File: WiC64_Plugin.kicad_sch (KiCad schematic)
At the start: 59 parts, among them CN1 USERPORT-C64, CN2 OLED0.96, Q1 BSS138, Q10 BSS138, Q11 BSS138, Q2 BSS138, Q3 BSS138, Q4 BSS138, Q5 BSS138, Q6 BSS138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

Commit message: Initial +4 version
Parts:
- removed CN1: USERPORT-C64, WiC64:UPS24CONN, symbol cbm-connectors:USERPORT-C64-CONN
- added CN1: PLUS4_USERPORT, WiC64:UPS24CONN, symbol PLUS4_USERPORT:PLUS4_USERPORT
- SW1: value RESET-C64 -> RESET
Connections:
- net +5V: now also CN1.2 (VCC)
- net FLAG2: now also Q8.3 (D), R16.2, CN1.H (~{DCD}); no longer Q1.3 (D), R2.2
- net GND: now also CN1.1 (GND), CN1.12 (GND), CN1.A (GND), CN1.N (GND)
- net IO14: now also Q4.2 (S), R7.2; no longer Q7.2 (S), R13.2
- net IO16: now also Q1.2 (S), R1.2; no longer Q2.2 (S), R3.2
- net IO17: now also Q11.2 (S), R21.2; no longer Q3.2 (S), R5.2
- net IO18: now also Q2.2 (S), R3.2; no longer Q4.2 (S), R7.2
- net IO21: now also Q7.2 (S), R13.2; no longer Q6.2 (S), R11.2
- net IO22: now also Q9.2 (S), R17.2; no longer Q8.2 (S), R15.2
- net IO23: now also Q10.2 (S), R19.2; no longer Q9.2 (S), R17.2
- net IO25: now also Q6.2 (S), R11.2; no longer Q10.2 (S), R19.2
- net IO26: now also Q8.2 (S), R15.2; no longer Q1.2 (S), R1.2
- net IO27: now also Q3.2 (S), R5.2; no longer Q11.2 (S), R21.2
- net PA2: now also Q3.3 (D), R6.2, CN1.D (~{RTS}); no longer Q11.3 (D), R22.2
- net PB0: now also Q1.3 (D), R2.2, CN1.B (D0); no longer Q2.3 (D), R4.2
- net PB1: now also Q11.3 (D), R22.2, CN1.K (D1); no longer Q3.3 (D), R6.2
- net PB2: now also Q2.3 (D), R4.2, CN1.4 (D2); no longer Q4.3 (D), R8.2
- net PB3: now also CN1.5 (D3)
- net PB4: now also Q7.3 (D), R14.2, CN1.6 (D4); no longer Q6.3 (D), R12.2
- net PB5: now also Q9.3 (D), R18.2, CN1.7 (D5); no longer Q8.3 (D), R16.2
- net PB6: now also Q10.3 (D), R20.2, CN1.J (D6); no longer Q9.3 (D), R18.2
- net PB7: now also Q6.3 (D), R12.2, CN1.F (D7); no longer Q10.3 (D), R20.2
- net PC2: now also Q4.3 (D), R8.2, CN1.E (~{DTR}); no longer Q7.3 (D), R14.2
- net at D4.3: now also CN1.10 (+9VAC)
- net at D4.4: now also CN1.11 (-9VAC)
- net at SW1.1: now also CN1.3 (~{RESET})
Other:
- note added: "+4->ESP"
- note added: "Control Signals Logic: - PC2 : Handshake: C64/+4 => ESP (ack/strobe: byte read from/written to port) (rising edge) - FLAG2: Handshake: ESP => C64/+4 (ack/strobe: byte read from/written to port) (falling edge) - PA2 : Direction: HIGH = C64/+4 => ESP, LOW = ESP => C64/+4 (Controlled by C64/+4)"
- note added: "ESP->+4"
- moved on the sheet: CN2, D3, JP2, SW1

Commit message: Complete changes for +4 version
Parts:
- added L1: FERRITE, WiC64:Ferrite_D6.0mm_L10.00mm_Horizontal, symbol Device:L_Ferrite
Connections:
- net +5V: now also L1.1; no longer CN1.2 (VCC)
- new net: CN1.2 (VCC), L1.2
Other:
- company: (none) -> SukkoPera
- title: WiC64 Plugin -> WiC+4
- moved on the sheet: D3, JP2
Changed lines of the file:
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@@
 	(paper "A4")
 	(title_block
-		(title "WiC64 Plugin")
-		(date "2024-05-26")
-		(rev "0.6-Sukko")
-		(comment 1 "(C) 2021 by GMP")
-		(comment 2 "Modified by SukkoPera 2024")
-		(comment 3 "https://github.com/SukkoPera/WiC64-Plus4")
+		(title "WiC+4")
+		(date "2024-06-02")
+		(rev "1git")
+		(company "SukkoPera")
+		(comment 1 "Based on C64 version by GMP 2021")
+		(comment 2 "https://github.com/SukkoPera/WiC64-Plus4")
 	)
 	(junction
@@
 	)
 	(junction
-		(at 107.95 93.98)
+		(at 101.6 93.98)
 		(diameter 0)
 		(color 0 0 0 0)
@@
 	(wire
 		(pts
-			(xy 96.52 87.63) (xy 96.52 90.17)
+			(xy 92.71 87.63) (xy 92.71 90.17)
 		)
 		(stroke
@@
 	(wire
 		(pts
-			(xy 107.95 93.98) (xy 107.95 88.9)
+			(xy 101.6 93.98) (xy 101.6 88.9)
 		)
 		(stroke
@@
 	(wire
 		(pts
-			(xy 107.95 93.98) (xy 128.27 93.98)
+			(xy 101.6 93.98) (xy 105.41 93.98)
 		)
 		(stroke
@@
 	(wire
 		(pts
-			(xy 102.87 93.98) (xy 107.95 93.98)
+			(xy 99.06 93.98) (xy 101.6 93.98)
 		)
 		(stroke
@@
 	(wire
 		(pts
-			(xy 83.82 93.98) (xy 90.17 93.98)
+			(xy 113.03 93.98) (xy 128.27 93.98)
+		)
+		(stroke
+			(width 0)
+			(type default)
+		)
+	)
+	(wire
+		(pts
+			(xy 83.82 93.98) (xy 86.36 93.98)
 		)
 		(stroke
@@
 	(wire
 		(pts
-			(xy 96.52 77.47) (xy 96.52 80.01)
+			(xy 92.71 77.47) (xy 92.71 80.01)
 		)
 		(stroke
@@
 	(text "ESP32 DEVKIT\nPOWER"
 		(exclude_from_sim no)
-		(at 96.52 67.564 0)
+		(at 92.71 67.564 0)
 		(effects
 			(font
@@
 	(symbol
 		(lib_id "power:+5V")
-		(at 107.95 88.9 0)
+		(at 101.6 88.9 0)
 		(unit 1)
 		(exclude_from_sim no)
@@
 		(dnp no)
 		(property "Reference" "#PWR028"
-			(at 107.95 92.71 0)
+			(at 101.6 92.71 0)
 			(effects
 				(font
@@
 		)
 		(property "Value" "+5V"
-			(at 108.331 84.5058 0)
+			(at 101.981 84.5058 0)
 			(effects
 				(font
@@
 		)
 		(property "Footprint" ""
-			(at 107.95 88.9 0)
+			(at 101.6 88.9 0)
 			(effects
 				(font
@@
 		)
 		(property "Datasheet" ""
-			(at 107.95 88.9 0)
+			(at 101.6 88.9 0)
 			(effects
 				(font
@@
 		)
 		(property "Description" ""
-			(at 107.95 88.9 0)
+			(at 101.6 88.9 0)
 			(effects
 				(font
@@
 		(on_board yes)
 		(dnp no)
+		(fields_autoplaced yes)
 		(property "Reference" "SW1"
-			(at 118.11 89.281 0)
+			(at 118.11 88.9 0)
 			(effects
 				(font
@@
 		)
 		(property "Value" "RESET"
-			(at 118.11 91.5924 0)
+			(at 118.11 91.44 0)
 			(effects
 				(font
@@
 	(symbol
 		(lib_id "Device:D_Schottky")
-		(at 96.52 83.82 270)
+		(at 92.71 83.82 270)
 		(unit 1)
 		(exclude_from_sim no)
@@
 		(dnp no)
 		(property "Reference" "D3"
-			(at 93.98 83.82 0)
+			(at 90.17 83.82 0)
 			(effects
 				(font
@@
 		)
 		(property "Value" "1N5819"
-			(at 99.695 83.82 0)
+			(at 95.885 83.82 0)
 			(effects
 				(font
@@
 		)
 		(property "Footprint" "Diode_SMD:D_SOD-123"
-			(at 96.52 83.82 0)
+			(at 92.71 83.82 0)
 			(effects
 				(font
@@
 		)
 		(property "Datasheet" "~"
-			(at 96.52 83.82 0)
+			(at 92.71 83.82 0)
 			(effects
 				(font
@@
 		)
 		(property "Description" ""
-			(at 96.52 83.82 0)
+			(at 92.71 83.82 0)
 			(effects
 				(font
@@
 		)
 		(property "LCSC" "C402219"
-			(at 96.52 83.82 0)
+			(at 92.71 83.82 0)
 			(effects
 				(font
@@
 	(symbol
 		(lib_id "power:VCC")
-		(at 96.52 77.47 0)
+		(at 92.71 77.47 0)
 		(unit 1)
 		(exclude_from_sim no)
@@
 		(fields_autoplaced yes)
 		(property "Reference" "#PWR036"
-			(at 96.52 81.28 0)
+			(at 92.71 81.28 0)
 			(effects
 				(font
@@
 		)
 		(property "Value" "VCC"
-			(at 96.52 72.39 0)
+			(at 92.71 72.39 0)
 			(effects
 				(font
@@
 		)
 		(property "Footprint" ""
-			(at 96.52 77.47 0)
+			(at 92.71 77.47 0)
 			(effects
 				(font
@@
 		)
 		(property "Datasheet" ""
-			(at 96.52 77.47 0)
+			(at 92.71 77.47 0)
 			(effects
 				(font
@@
 		)
 		(property "Description" "Power symbol creates a global label with name \"VCC\""
-			(at 96.52 77.47 0)
+			(at 92.71 77.47 0)
 			(effects
 				(font
@@
 	(symbol
 		(lib_id "Jumper:Jumper_3_Open")
-		(at 96.52 93.98 180)
+		(at 92.71 93.98 180)
 		(unit 1)
 		(exclude_from_sim yes)
@@
 		(fields_autoplaced yes)
 		(property "Reference" "JP2"
-			(at 96.52 97.79 0)
+			(at 92.71 97.79 0)
 			(effects
 				(font
@@
 		)
 		(property "Value" "JMP_ESP_POWER"
-			(at 96.52 100.33 0)
+			(at 92.71 100.33 0)
 			(effects
 				(font
@@
 		)
 		(property "Footprint" "Jumper:SolderJumper-3_P1.3mm_Open_RoundedPad1.0x1.5mm"
-			(at 96.52 93.98 0)
+			(at 92.71 93.98 0)
 			(effects
 				(font
@@
 		)
 		(property "Datasheet" "~"
-			(at 96.52 93.98 0)
+			(at 92.71 93.98 0)
 			(effects
 				(font
@@
 		)
 		(property "Description" "Jumper, 3-pole, both open"
-			(at 96.52 93.98 0)
+			(at 92.71 93.98 0)
 			(effects
 				(font
@@
 					(unit 1)
 				)
+			)
+		)
+	)
+	(symbol
+		(lib_id "Device:L_Ferrite")
+		(at 109.22 93.98 90)
+		(unit 1)
+		(exclude_from_sim no)
+		(in_bom yes)
+		(on_board yes)
+		(dnp no)
+		(fields_autoplaced yes)
+		(property "Reference" "L1"
+			(at 109.22 87.63 90)
+			(effects
+				(font
+					(size 1.27 1.27)
+				)
+			)
+		)
+		(property "Value" "FERRITE"
+			(at 109.22 90.17 90)
+			(effects
+				(font
+					(size 1.27 1.27)
+				)
+			)
+		)
+		(property "Footprint" "WiC64:Ferrite_D6.0mm_L10.00mm_Horizontal"
+			(at 109.22 93.98 0)
+			(effects
+				(font
+					(size 1.27 1.27)
+				)
+				(hide yes)
+			)
+		)
+		(property "Datasheet" "~"
+			(at 109.22 93.98 0)
+			(effects
+				(font
+					(size 1.27 1.27)
+				)
+				(hide yes)
+			)
+		)
+		(property "Description" "Inductor with ferrite core"
+			(at 109.22 93.98 0)
+			(effects
+				(font
+					(size 1.27 1.27)
+				)
+				(hide yes)
+			)
+		)
+		(pin "2"
+		)
+		(pin "1"
+		)
+		(instances
+			(project "WiC64_Plugin"
+				(path "/1ea654e4-7839-493d-a83b-1258d630b489"
+					(reference "L1")
+					(unit 1)
+				)

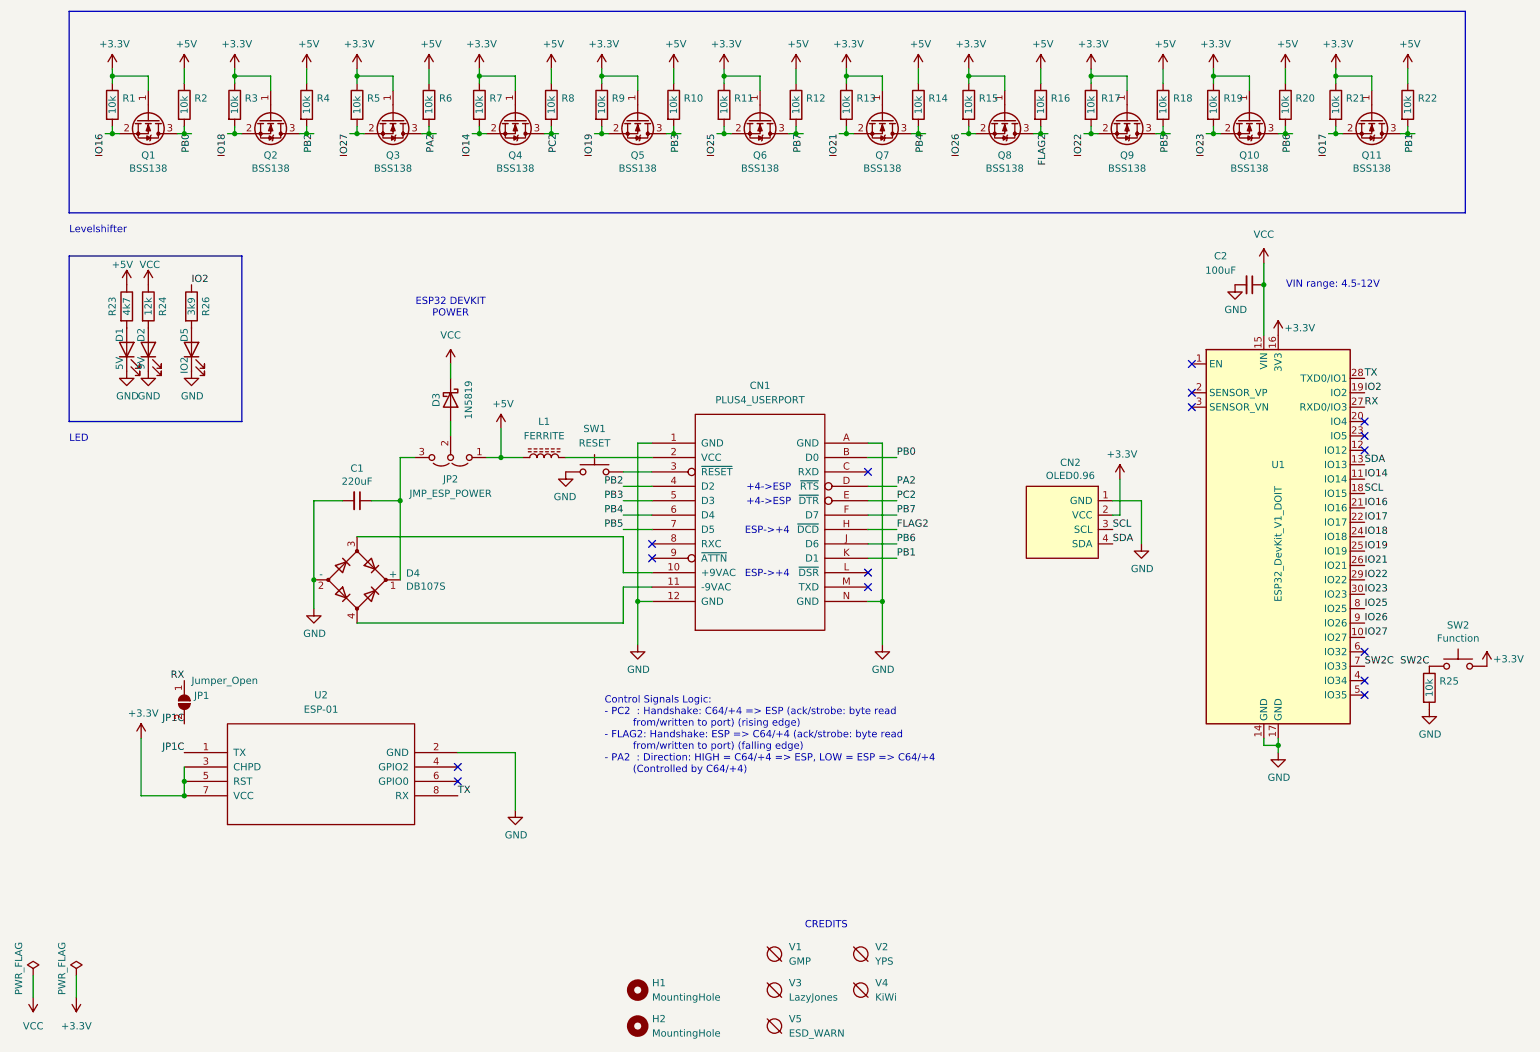
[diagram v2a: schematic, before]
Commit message: Latch FLAG2
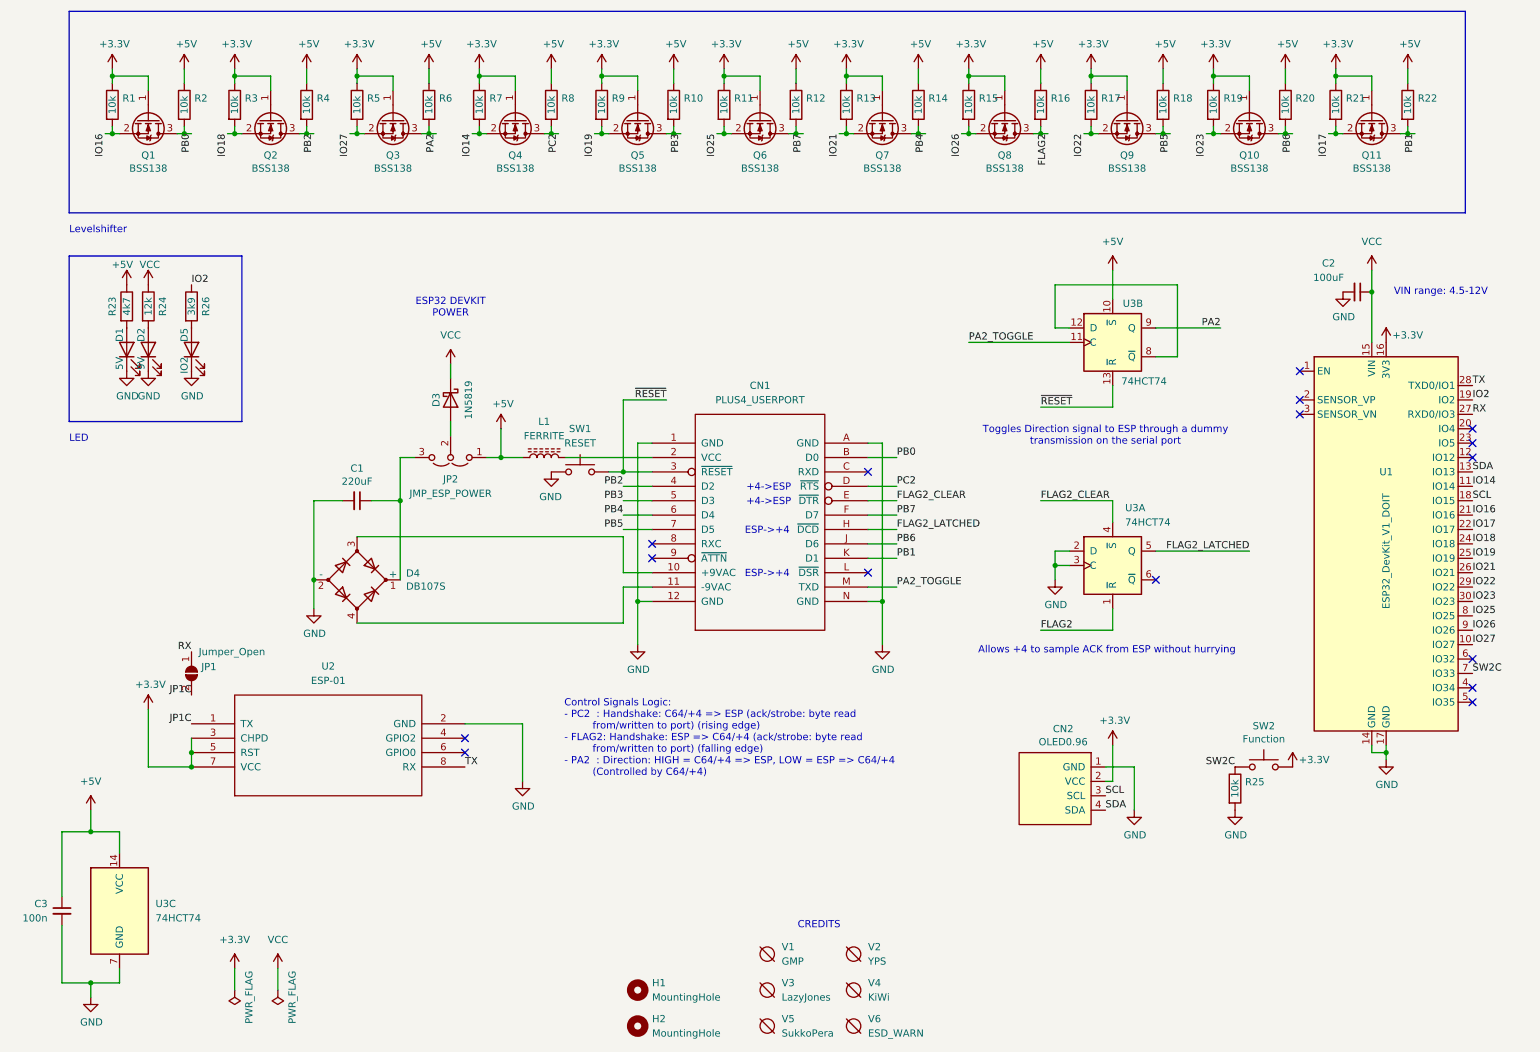
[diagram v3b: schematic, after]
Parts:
- added C3: 100n, Capacitor_SMD:C_0805_2012Metric_Pad1.18x1.45mm_HandSolder, symbol Device:C_Small
- added U3: 74HCT74, Package_SO:SOIC-14_3.9x8.7mm_P1.27mm, symbol 74xx:74HCT74
- added V5: SukkoPera, WiC64:PearLogo, symbol void:Void
- V1, V2, V3, V4: now left out of the parts list
- V6: renamed from V5; now left out of the parts list
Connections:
- net +5V: now also C3.1, U3.10 (~{S}), U3.14 (VCC)
- net FLAG2: now also U3.1 (~{R}); no longer CN1.H (~{DCD})
- net GND: now also C3.2, U3.2 (D), U3.3 (C), U3.7 (GND)
- net PA2: now also U3.9 (Q); no longer CN1.D (~{RTS})
- net PC2: now also CN1.D (~{RTS}); no longer CN1.E (~{DTR})
- net ~{RESET}: now reaches CN1.3 (~{RESET}), SW1.1
- net ~{RESET}: now also U3.13 (~{R})
- net PA2_TOGGLE: now reaches CN1.M (TXD)
- net PA2_TOGGLE: now also U3.11 (C)
- new net: U3.12 (D), U3.8 (~{Q})
- new net FLAG2_CLEAR: CN1.E (~{DTR}), U3.4 (~{S})
- new net FLAG2_LATCHED: CN1.H (~{DCD}), U3.5 (Q)
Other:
- note added: "Allows +4 to sample ACK from ESP without hurrying"
- note added: "Toggles Direction signal to ESP through a dummy transmission on the serial port"
- moved on the sheet: C2, CN2, JP1, R25, SW1, SW2, U1, U2, V1, V2, V3, V4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
